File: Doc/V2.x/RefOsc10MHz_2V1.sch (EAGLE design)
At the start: 81 parts, among them CON1 TYCO-AMP_USBUSB-B_SMT, CON2 HEADER-2X5SMD, CON3 SD-73100-0105, CON4 AVR-ISP-6SMD, CON5 AVR-JTAG-10SMD, CON6 HEADER-2X3SMD, CON7 MCX-J-P-X-RA-SM1, IC1 ATmega328-P, IC2 LC4032V_XXT44, IC3 74HCT221D, IC6 LM2831YMF, IC7 CFPT-141, IC8 712-RXM-GNSS-TM-B, U5 OPA354

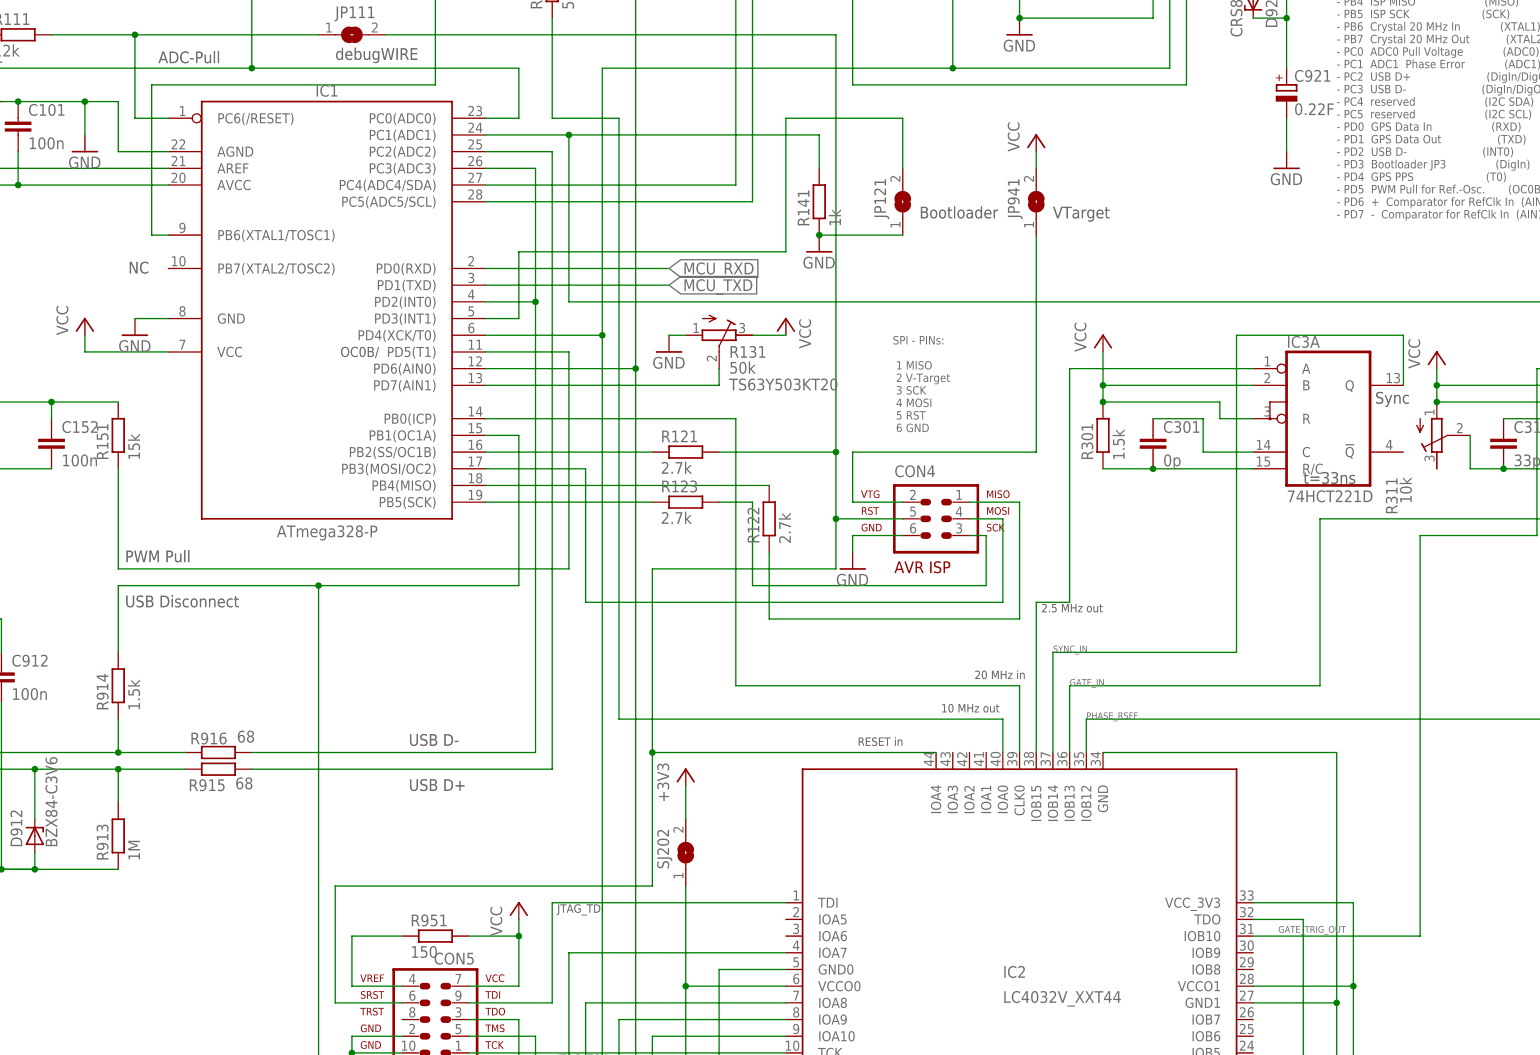
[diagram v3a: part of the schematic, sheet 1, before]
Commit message: avr_DF4IAH_Bootloader - Doc - Eagle: V2.1 - PWM-Pull - drive not direct from AVR with unstabilized 5.0V but by the CPLD with its stabilized 3.3V instead.
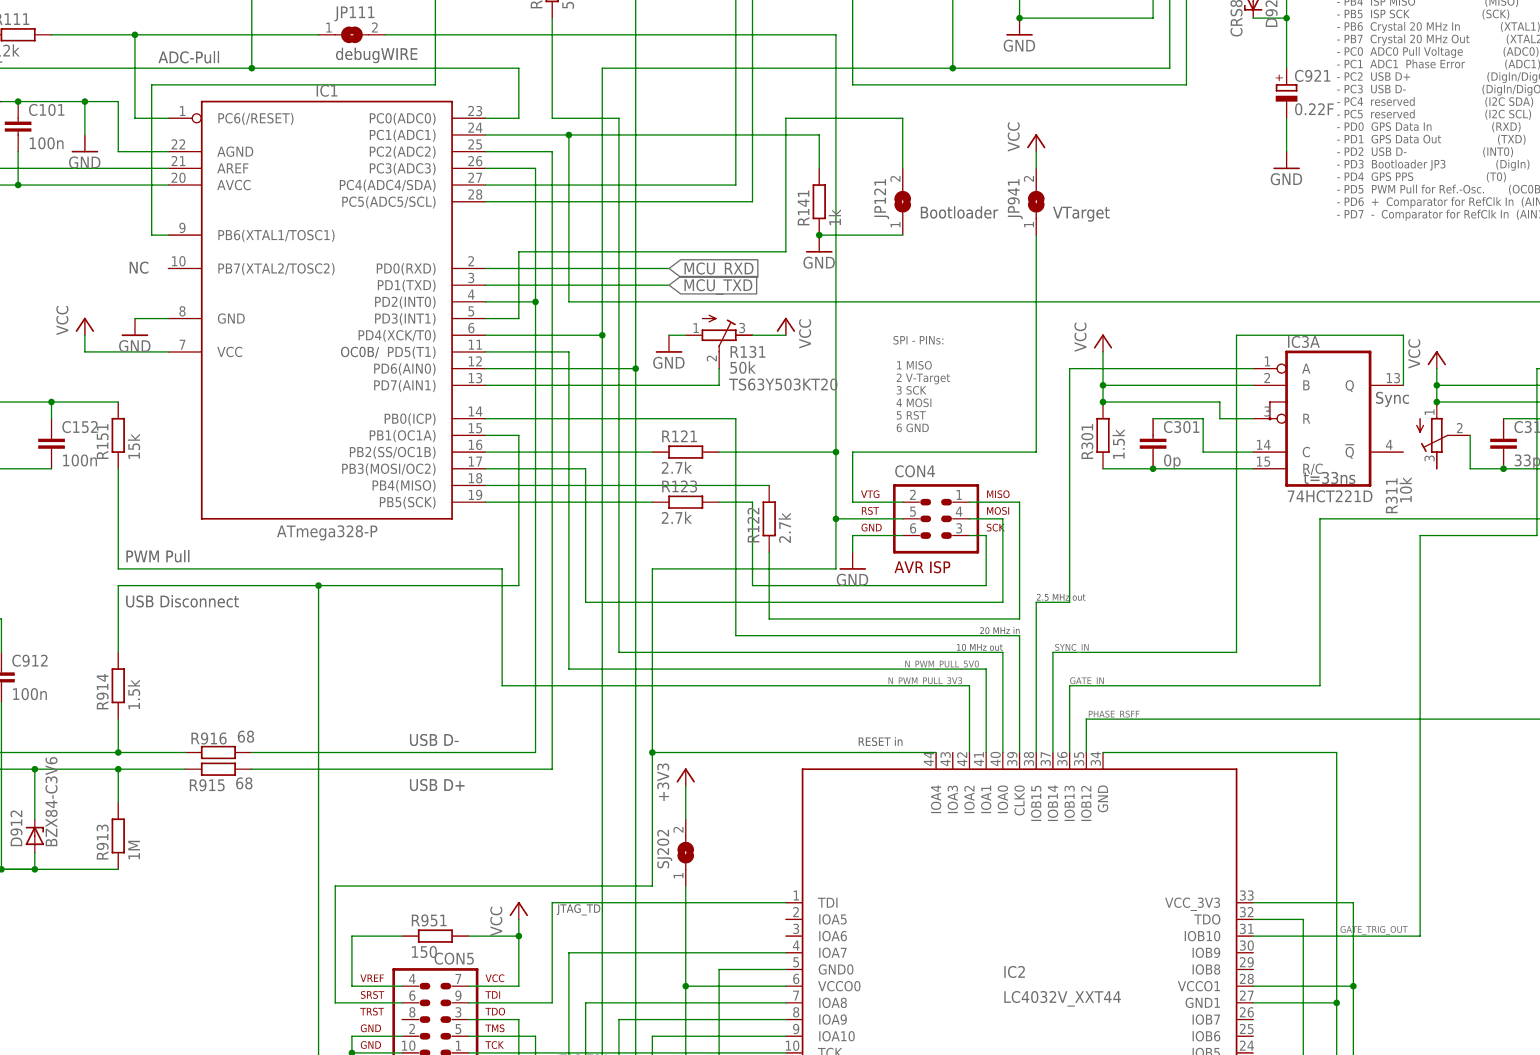
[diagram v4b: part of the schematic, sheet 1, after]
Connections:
- removed net N_PWM_PULL: IC1.PD5(T1), R151.1
- new net N_PWM_PULL_3V3: IC2.IOA2, R151.1
- new net N_PWM_PULL_5V0: IC1.PD5(T1), IC2.IOA1
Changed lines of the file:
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@@
 <text x="294.386" y="129.794" size="1.778" layer="97">t=362ns</text>
 <text x="305.562" y="239.776" size="1.778" layer="97">IC-Supplies</text>
-<text x="193.802" y="100.076" size="1.27" layer="97">20 MHz in</text>
-<text x="188.722" y="94.996" size="1.27" layer="97">10 MHz out</text>
-<text x="203.962" y="110.236" size="1.27" layer="97">2.5 MHz out</text>
+<text x="194.564" y="106.934" size="1.016" layer="97">20 MHz in</text>
+<text x="191.008" y="104.394" size="1.016" layer="97">10 MHz out</text>
+<text x="203.2" y="112.014" size="1.016" layer="97">2.5 MHz out</text>
 <text x="10.414" y="258.826" size="2.54" layer="97">DF4IAH  10 MHz Reference Oscillator
 V 2.1</text>
@@
 <pinref part="IC1" gate="G$1" pin="PB0(ICP)"/>
 <wire x1="119.38" y1="139.7" x2="157.48" y2="139.7" width="0.1524" layer="91"/>
-<wire x1="157.48" y1="139.7" x2="157.48" y2="99.06" width="0.1524" layer="91"/>
-<wire x1="157.48" y1="99.06" x2="200.66" y2="99.06" width="0.1524" layer="91"/>
-<wire x1="200.66" y1="99.06" x2="200.66" y2="88.9" width="0.1524" layer="91"/>
+<wire x1="157.48" y1="139.7" x2="157.48" y2="106.68" width="0.1524" layer="91"/>
+<wire x1="157.48" y1="106.68" x2="200.66" y2="106.68" width="0.1524" layer="91"/>
+<wire x1="200.66" y1="106.68" x2="200.66" y2="88.9" width="0.1524" layer="91"/>
 <pinref part="IC2" gate="G$1" pin="CLK0"/>
 </segment>
@@
 </segment>
 </net>
-<net name="N_PWM_PULL" class="0">
-<segment>
-<wire x1="132.08" y1="116.84" x2="63.5" y2="116.84" width="0.1524" layer="91"/>
-<wire x1="63.5" y1="116.84" x2="63.5" y2="132.08" width="0.1524" layer="91"/>
+<net name="N_PWM_PULL_5V0" class="0">
+<segment>
 <pinref part="IC1" gate="G$1" pin="PD5(T1)"/>
 <wire x1="132.08" y1="149.86" x2="119.38" y2="149.86" width="0.1524" layer="91"/>
-<wire x1="132.08" y1="116.84" x2="132.08" y2="149.86" width="0.1524" layer="91"/>
-<pinref part="R151" gate="G$1" pin="1"/>
+<wire x1="132.08" y1="101.6" x2="132.08" y2="149.86" width="0.1524" layer="91"/>
+<pinref part="IC2" gate="G$1" pin="IOA1"/>
+<wire x1="132.08" y1="101.6" x2="195.58" y2="101.6" width="0.1524" layer="91"/>
+<wire x1="195.58" y1="101.6" x2="195.58" y2="88.9" width="0.1524" layer="91"/>
+<label x="183.134" y="101.854" size="1.016" layer="95"/>
 </segment>
 </net>
@@
 <pinref part="IC3" gate="B" pin="Q"/>
 <pinref part="IC2" gate="G$1" pin="IOB13"/>
-<label x="208.28" y="99.06" size="1.016" layer="95"/>
+<label x="208.28" y="99.314" size="1.016" layer="95"/>
 </segment>
 </net>
@@
 <wire x1="139.7" y1="185.42" x2="129.54" y2="185.42" width="0.1524" layer="91"/>
 <wire x1="129.54" y1="185.42" x2="129.54" y2="200.66" width="0.1524" layer="91"/>
-<wire x1="139.7" y1="185.42" x2="139.7" y2="93.98" width="0.1524" layer="91"/>
-<wire x1="139.7" y1="93.98" x2="198.12" y2="93.98" width="0.1524" layer="91"/>
-<wire x1="198.12" y1="93.98" x2="198.12" y2="88.9" width="0.1524" layer="91"/>
+<wire x1="139.7" y1="185.42" x2="139.7" y2="104.14" width="0.1524" layer="91"/>
+<wire x1="139.7" y1="104.14" x2="198.12" y2="104.14" width="0.1524" layer="91"/>
+<wire x1="198.12" y1="104.14" x2="198.12" y2="88.9" width="0.1524" layer="91"/>
 <pinref part="IC2" gate="G$1" pin="IOA0"/>
 <pinref part="R931" gate="G$1" pin="1"/>
@@
 <pinref part="IC3" gate="A" pin="Q"/>
 <pinref part="IC2" gate="G$1" pin="IOB14"/>
-<label x="205.74" y="104.14" size="1.016" layer="95"/>
+<label x="205.994" y="104.394" size="1.016" layer="95"/>
 </segment>
 </net>
@@
 <wire x1="261.62" y1="121.92" x2="261.62" y2="60.96" width="0.1524" layer="91"/>
 <wire x1="261.62" y1="60.96" x2="236.22" y2="60.96" width="0.1524" layer="91"/>
-<label x="240.03" y="61.468" size="1.016" layer="95"/>
+<label x="249.428" y="61.468" size="1.016" layer="95"/>
 </segment>
 </net>
@@
 <pinref part="IC2" gate="G$1" pin="IOB12"/>
 <wire x1="210.82" y1="93.98" x2="304.8" y2="93.98" width="0.1524" layer="91"/>
-<label x="210.82" y="93.98" size="1.016" layer="95"/>
+<label x="211.074" y="94.234" size="1.016" layer="95"/>
 <pinref part="D401" gate="G$1" pin="A"/>
 </segment>
@@
 </segment>
 </net>
+<net name="N_PWM_PULL_3V3" class="0">
+<segment>
+<pinref part="R151" gate="G$1" pin="1"/>
+<wire x1="63.5" y1="116.84" x2="63.5" y2="132.08" width="0.1524" layer="91"/>
+<wire x1="63.5" y1="116.84" x2="121.92" y2="116.84" width="0.1524" layer="91"/>
+<wire x1="121.92" y1="116.84" x2="121.92" y2="99.06" width="0.1524" layer="91"/>
+<wire x1="121.92" y1="99.06" x2="193.04" y2="99.06" width="0.1524" layer="91"/>
+<pinref part="IC2" gate="G$1" pin="IOA2"/>
+<wire x1="193.04" y1="99.06" x2="193.04" y2="88.9" width="0.1524" layer="91"/>
+<label x="180.594" y="99.314" size="1.016" layer="95"/>
+</segment>
+</net>

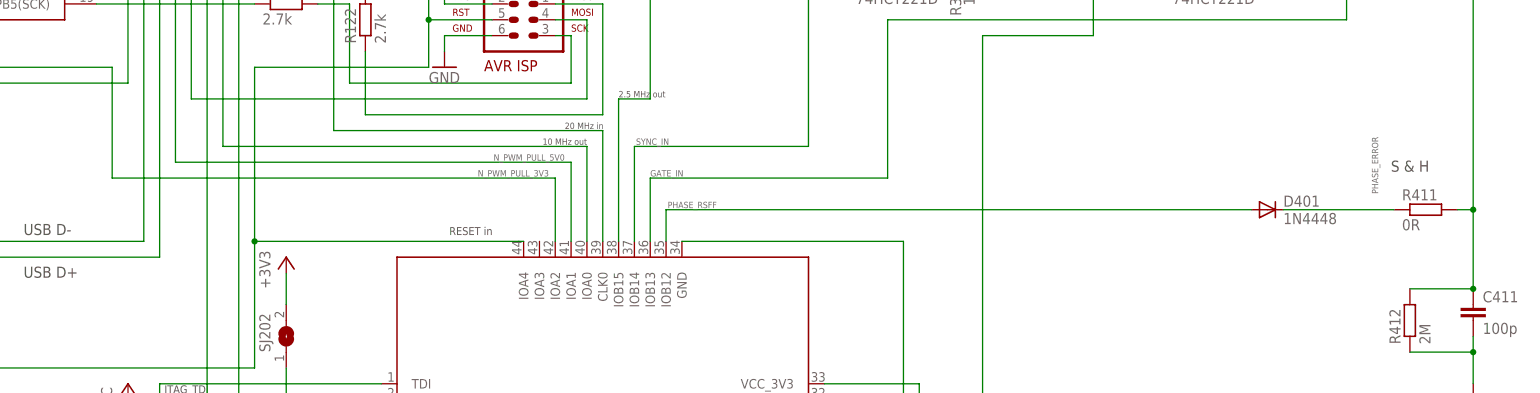
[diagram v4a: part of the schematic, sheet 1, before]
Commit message: avr_DF4IAH_Bootloader - Doc - Eagle: V2.1 - R411 modified, CPLD pinout changed
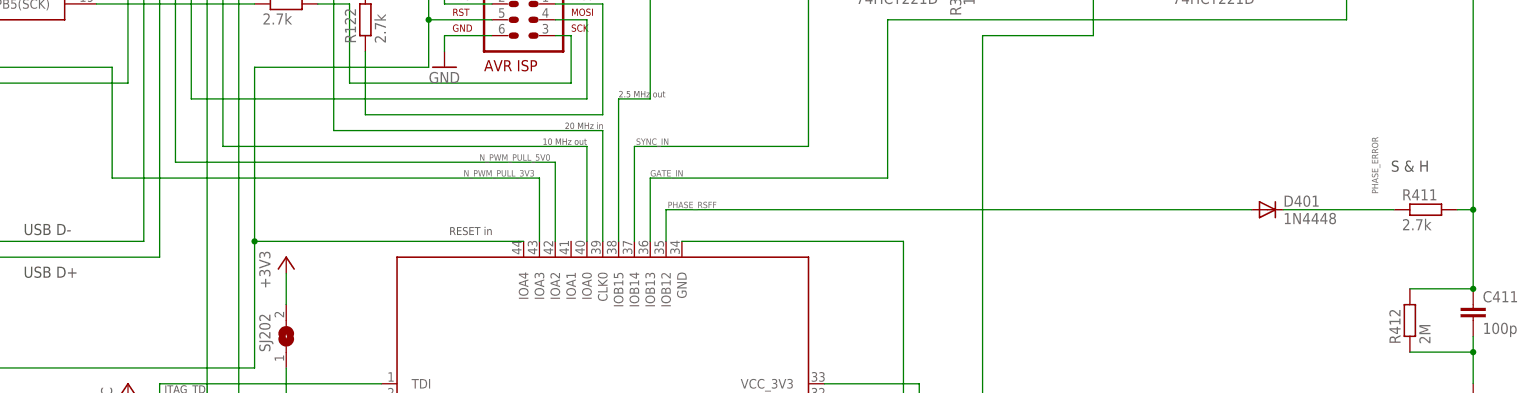
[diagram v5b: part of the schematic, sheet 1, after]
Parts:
- R411: value 0R -> 2.7k
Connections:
- net N_PWM_PULL_3V3: now also IC2.IOA3; no longer IC2.IOA2
- net N_PWM_PULL_5V0: now also IC2.IOA2; no longer IC2.IOA1
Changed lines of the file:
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@@
 <part name="R111" library="rcl" deviceset="R-EU_" device="R0805" value="12k"/>
 <part name="R931" library="rcl" deviceset="R-EU_" device="R0805" value="51"/>
-<part name="R411" library="rcl" deviceset="R-EU_" device="R0805" value="0R"/>
+<part name="R411" library="rcl" deviceset="R-EU_" device="R0805" value="2.7k"/>
 <part name="R141" library="rcl" deviceset="R-EU_" device="R0805" value="1k"/>
 <part name="R301" library="rcl" deviceset="R-EU_" device="R0805" value="1.5k"/>
@@
 <wire x1="132.08" y1="149.86" x2="119.38" y2="149.86" width="0.1524" layer="91"/>
 <wire x1="132.08" y1="101.6" x2="132.08" y2="149.86" width="0.1524" layer="91"/>
-<pinref part="IC2" gate="G$1" pin="IOA1"/>
-<wire x1="132.08" y1="101.6" x2="195.58" y2="101.6" width="0.1524" layer="91"/>
-<wire x1="195.58" y1="101.6" x2="195.58" y2="88.9" width="0.1524" layer="91"/>
-<label x="183.134" y="101.854" size="1.016" layer="95"/>
+<wire x1="132.08" y1="101.6" x2="193.04" y2="101.6" width="0.1524" layer="91"/>
+<label x="180.848" y="101.854" size="1.016" layer="95"/>
+<pinref part="IC2" gate="G$1" pin="IOA2"/>
+<wire x1="193.04" y1="101.6" x2="193.04" y2="88.9" width="0.1524" layer="91"/>
 </segment>
 </net>
@@
 <wire x1="63.5" y1="116.84" x2="121.92" y2="116.84" width="0.1524" layer="91"/>
 <wire x1="121.92" y1="116.84" x2="121.92" y2="99.06" width="0.1524" layer="91"/>
-<wire x1="121.92" y1="99.06" x2="193.04" y2="99.06" width="0.1524" layer="91"/>
-<pinref part="IC2" gate="G$1" pin="IOA2"/>
-<wire x1="193.04" y1="99.06" x2="193.04" y2="88.9" width="0.1524" layer="91"/>
-<label x="180.594" y="99.314" size="1.016" layer="95"/>
-</segment>
-</net>
+<wire x1="121.92" y1="99.06" x2="190.5" y2="99.06" width="0.1524" layer="91"/>
+<label x="178.308" y="99.314" size="1.016" layer="95"/>
+<pinref part="IC2" gate="G$1" pin="IOA3"/>
+<wire x1="190.5" y1="99.06" x2="190.5" y2="88.9" width="0.1524" layer="91"/>
+</segment>
+</net>
